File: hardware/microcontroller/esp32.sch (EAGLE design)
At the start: 20 parts, among them IC1 ESP32-WROOM-32U, IC2 AMS1117-1.5

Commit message: ESP32 Schematic clean-up
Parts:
- removed J3: (no value), con-amp:MTA06-100
- added UPLOAD_PROGRAMME: (no value), con-amp:MTA06-156
- GSM: device con-amp:MTA04-156 -> con-amp:MTA05-156
- RFID: device con-amp:MTA08-100 -> con-amp:MTA08-156
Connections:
- new net GSM_VCC: GSM.5, GSM_VCC.1
- net GND: now also GSM.4, UPLOAD_PROGRAMME.6; no longer GSM.3, J3.6
- net GSM_RESET: now also GSM.3; no longer GSM.4, GSM_VCC.1
- net RX: now also UPLOAD_PROGRAMME.2; no longer J3.2
- net TX: now also UPLOAD_PROGRAMME.3; no longer J3.3
- net VCC: now also UPLOAD_PROGRAMME.4; no longer J3.4
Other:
- note added: "BOOT, ENABLE, Programming Pins"
- note added: "ESP32"
- note added: "ESP32_Base"
- note added: "LCD, GSM, RFID, GSM external Power"
- note added: "Power 5V to 3.3V"
- moved on the sheet: BOOT, C1, C2, C5, D1, EN, GSM_VCC, IC1, IC2, LCD, POWER, R1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

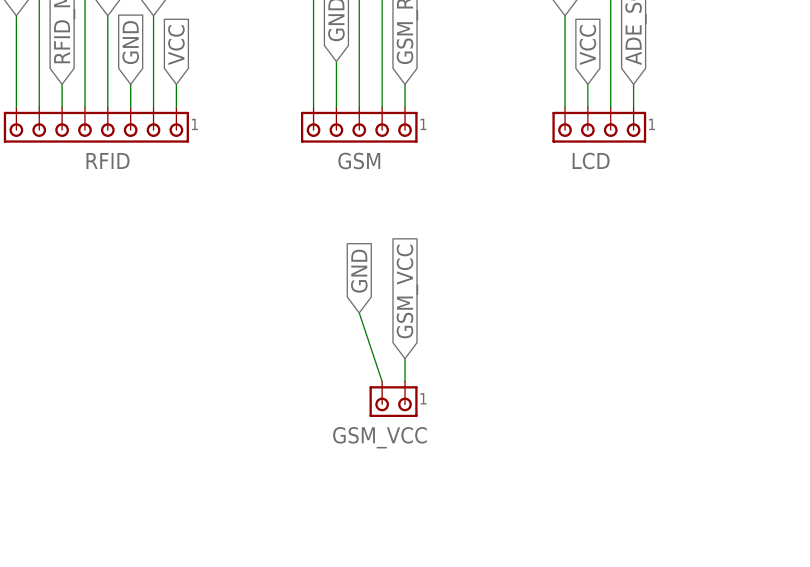
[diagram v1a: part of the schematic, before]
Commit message: ESP32 Schematic and Board Cleanup
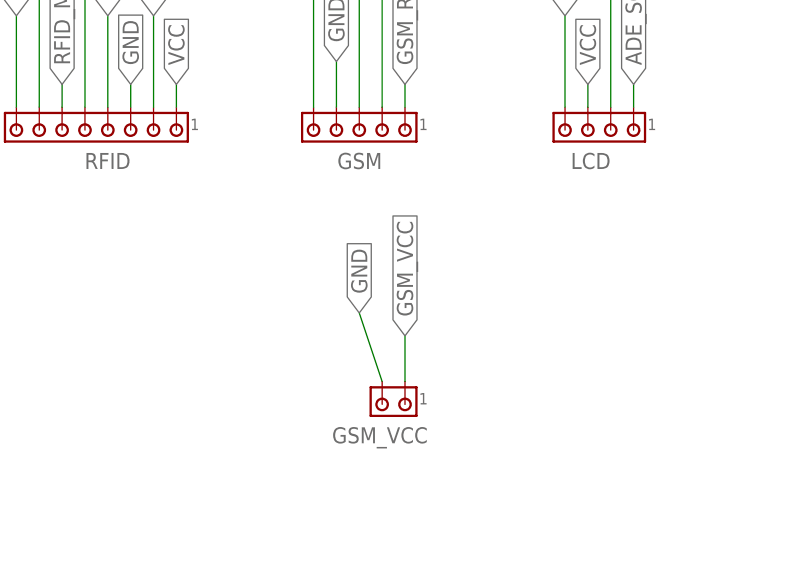
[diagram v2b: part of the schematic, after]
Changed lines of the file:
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@@
 <segment>
 <pinref part="GSM_VCC" gate="G$1" pin="1"/>
-<label x="223.52" y="-45.72" size="1.778" layer="95" rot="R90" xref="yes"/>
-<wire x1="223.52" y1="-45.72" x2="223.52" y2="-48.26" width="0.1524" layer="91"/>
+<label x="223.52" y="-43.18" size="1.778" layer="95" rot="R90" xref="yes"/>
+<wire x1="223.52" y1="-43.18" x2="223.52" y2="-48.26" width="0.1524" layer="91"/>
 </segment>
 </net>

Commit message: ESP32_Final Design
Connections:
- removed net REID_MISO: RFID.5
- net RFID_MISO: now also RFID.5
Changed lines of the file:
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@@
 <net name="RFID_MOSI" class="0">
 <segment>
-<label x="185.42" y="-15.24" size="1.778" layer="95" rot="R90" xref="yes"/>
+<label x="185.42" y="-12.7" size="1.778" layer="95" rot="R90" xref="yes"/>
 <pinref part="RFID" gate="G$2" pin="6"/>
-<wire x1="185.42" y1="-15.24" x2="185.42" y2="-17.78" width="0.1524" layer="91"/>
+<wire x1="185.42" y1="-12.7" x2="185.42" y2="-17.78" width="0.1524" layer="91"/>
 </segment>
 <segment>
@@
 <segment>
 <pinref part="U$1" gate="G$1" pin="16"/>
-<wire x1="48.26" y1="10.16" x2="48.26" y2="7.62" width="0.1524" layer="91"/>
-<label x="48.26" y="7.62" size="1.778" layer="95" rot="R270" xref="yes"/>
-</segment>
-</net>
-<net name="REID_MISO" class="0">
-<segment>
-<label x="187.96" y="7.62" size="1.778" layer="95" rot="R90" xref="yes"/>
-<pinref part="RFID" gate="G$2" pin="5"/>
-<wire x1="187.96" y1="7.62" x2="187.96" y2="-17.78" width="0.1524" layer="91"/>
+<wire x1="48.26" y1="10.16" x2="48.26" y2="5.08" width="0.1524" layer="91"/>
+<label x="48.26" y="5.08" size="1.778" layer="95" rot="R270" xref="yes"/>
 </segment>
 </net>
@@
 <segment>
 <pinref part="U$1" gate="G$1" pin="14"/>
-<wire x1="27.94" y1="20.32" x2="25.4" y2="20.32" width="0.1524" layer="91"/>
-<label x="25.4" y="20.32" size="1.778" layer="95" rot="R180" xref="yes"/>
+<wire x1="27.94" y1="20.32" x2="20.32" y2="20.32" width="0.1524" layer="91"/>
+<label x="20.32" y="20.32" size="1.778" layer="95" rot="R180" xref="yes"/>
+</segment>
+<segment>
+<pinref part="RFID" gate="G$2" pin="5"/>
+<wire x1="187.96" y1="-17.78" x2="187.96" y2="7.62" width="0.1524" layer="91"/>
+<label x="187.96" y="7.62" size="1.778" layer="95" rot="R90" xref="yes"/>
 </segment>
 </net>
